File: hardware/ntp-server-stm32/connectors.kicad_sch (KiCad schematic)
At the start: 31 parts, among them J10 Conn_01x02_Pin, J11 Conn_01x08_Pin, J2 Conn_01x04_Pin, J3 Conn_01x06_Pin, J4 Conn_01x14_Pin, J5 USB4120-03-C_REVA6, J6 DE9_Socket_MountingHoles, J7 Conn_Coaxial, J8 Conn_Coaxial, J9 Conn_Coaxial, U15 TPD4E02B04DQAR, U16 TPD4E02B04DQAR, U17 TPD4E05U06DQAR, U18 TPD4E05U06DQAR, U19 TPD4E02B04DQAR, U20 TPD4E02B04DQAR

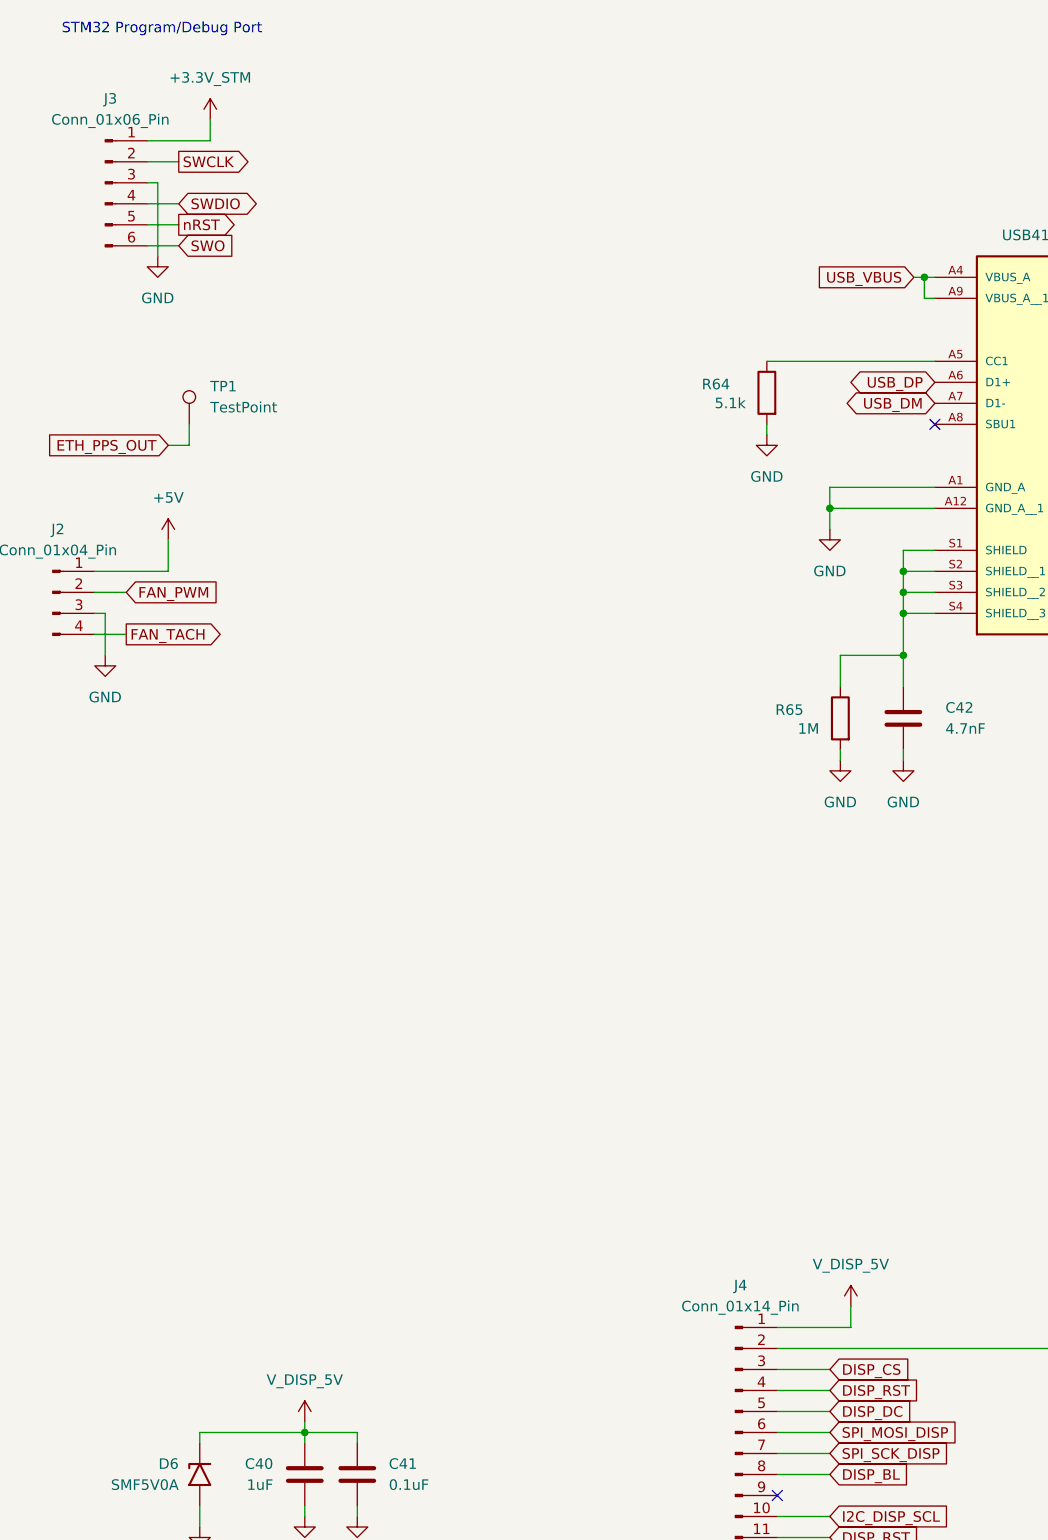
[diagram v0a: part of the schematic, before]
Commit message: Standardize net/rail names: plain 3V3 style, _N active-low, voltage-format PG/alerts
22 net renames applied across all sheets and verified: removed/added net-name
sets match intent exactly and all node connectivity is preserved (kicad-cli
netlist re-parse).

Co-Authored-By: Claude Opus 4.8 (1M context) <noreply@anthropic.com>
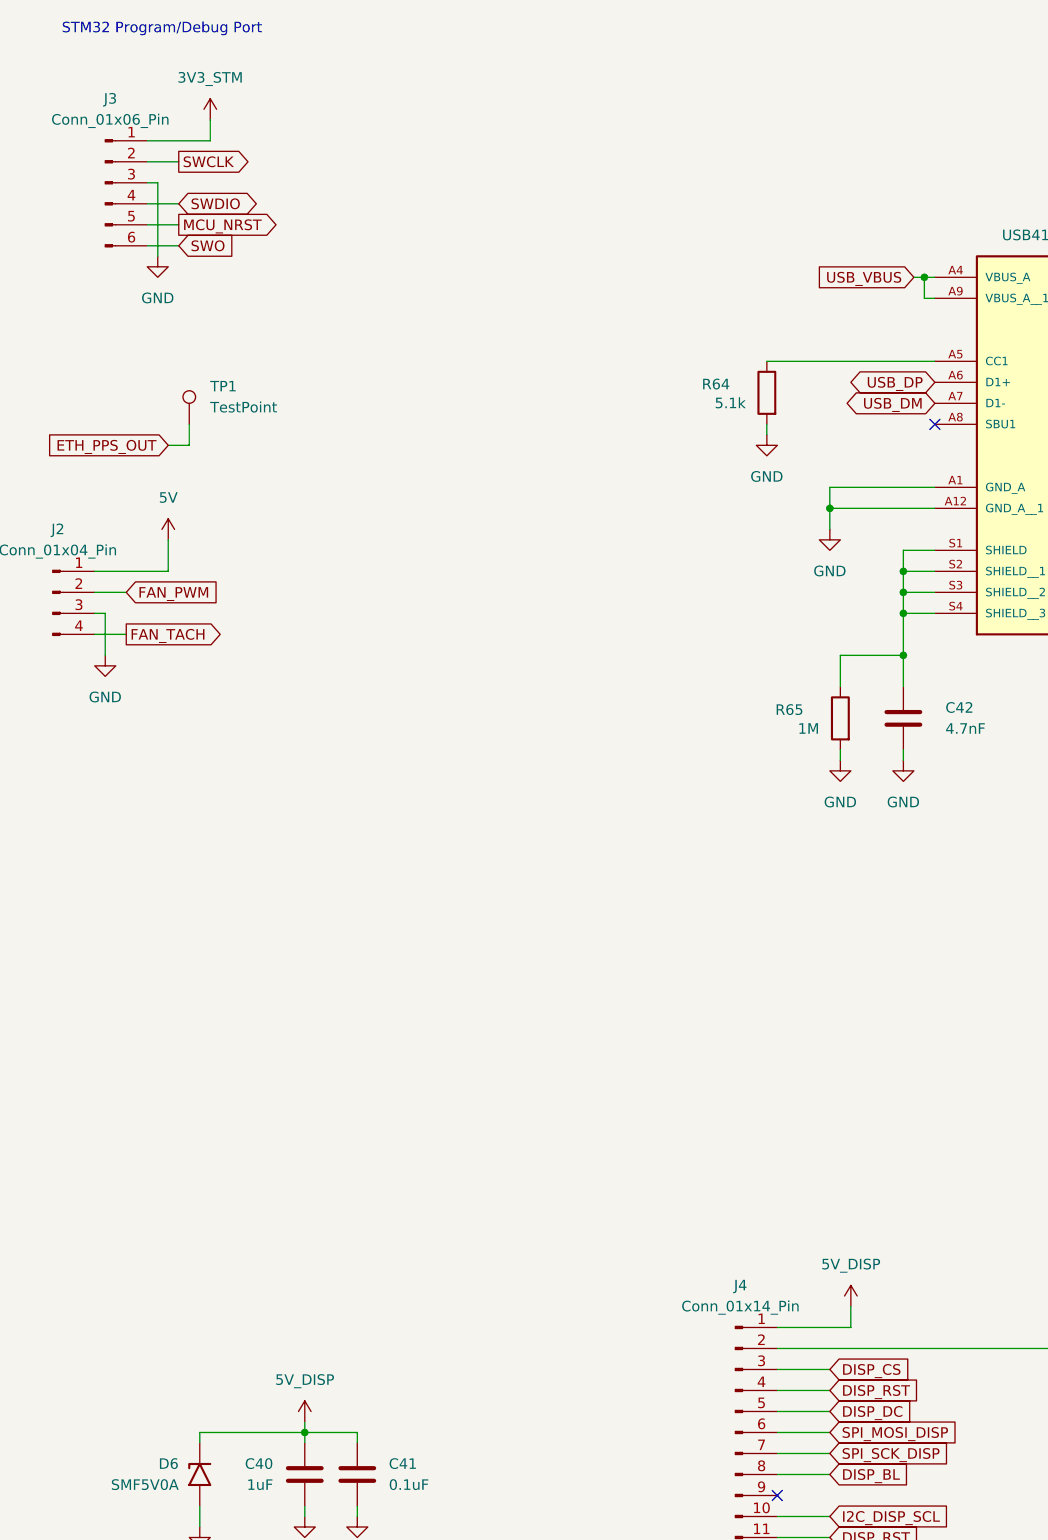
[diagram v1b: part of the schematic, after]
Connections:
- net +3.3V_STM renamed 3V3_STM
- net +5V renamed 5V
- net V_DISP_5V renamed 5V_DISP
- net nRST renamed MCU_NRST
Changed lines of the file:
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@@
 		)
 	)
-	(global_label "nRST"
+	(global_label "MCU_NRST"
 		(shape output)
 		(at 36.83 45.72 0)
@@
 			)
 		)
-		(property "Value" "+5V"
+		(property "Value" "5V"
 			(at 35.56 78.74 0)
 			(show_name no)
@@
 			)
 		)
-		(property "Value" "V_DISP_5V"
+		(property "Value" "5V_DISP"
 			(at 118.11 171.45 0)
 			(show_name no)
@@
 			)
 		)
-		(property "Value" "V_DISP_5V"
+		(property "Value" "5V_DISP"
 			(at 52.07 185.42 0)
 			(show_name no)
@@
 			)
 		)
-		(property "Value" "+3.3V_STM"
+		(property "Value" "3V3_STM"
 			(at 40.64 27.94 0)
 			(show_name no)

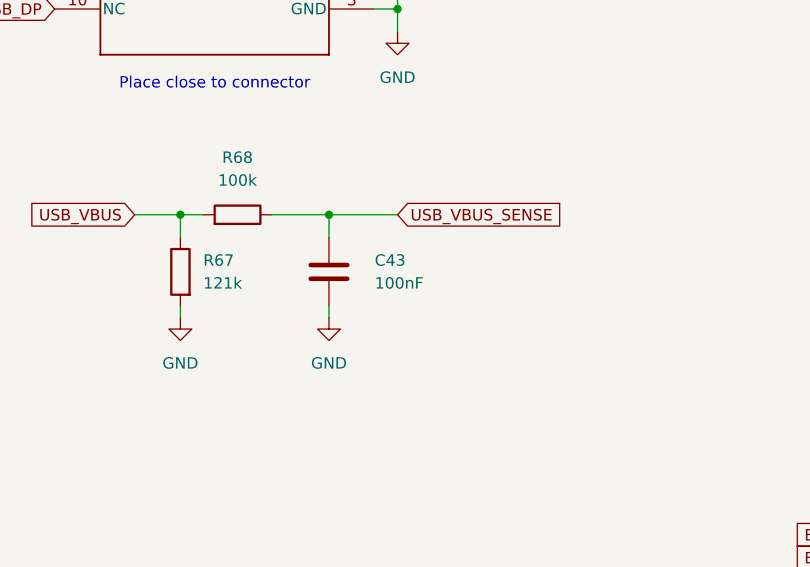
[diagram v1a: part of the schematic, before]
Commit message: Standardize + complete BOM; write fields back into KiCad symbols
- New sts1000_bom.csv: rebuilt from authoritative Value field (source MPN/footprint/
  description were corrupted by copy-paste). 338 standardized, 78 MPN-from-value,
  50 kept, ~64 flagged (SELECT/REVIEW-HV/SHUNT-REVIEW) each with full spec.
- Resistors -> deterministic Panasonic ERJ-2RKF 0402 1% 1/10W (consolidated 1 part/value).
- Caps -> verified Murata GRM parts where value matches; clean spec + footprint otherwise.
- 1633 symbol field updates (Value/Footprint/Description/MPN/Mfr/Digikey) written to
  .kicad_sch; netlist re-parse confirms connectivity byte-identical.
- Add docs/sts1000_net_naming.md naming reference.

Co-Authored-By: Claude Opus 4.8 (1M context) <noreply@anthropic.com>
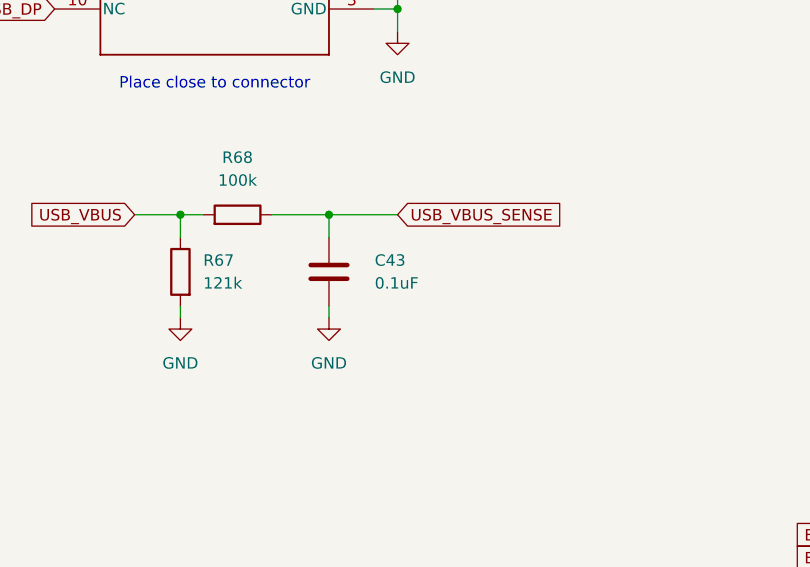
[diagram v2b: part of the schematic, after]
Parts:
- C40: footprint (none) -> C_0603_1608Metric
- C41: footprint (none) -> C_0402_1005Metric; DIGIKEY_PART_NUMBER (none) -> 490-6328-2-ND; MANUFACTURER (none) -> Murata; MANUFACTURER_PART_NUMBER (none) -> GRM155R71C104KA88J
- C42: footprint 0805 -> C_0402_1005Metric; DIGIKEY_PART_NUMBER 445-5972-1-ND -> 490-6334-2-ND; MANUFACTURER TDK -> Murata; MANUFACTURER_PART_NUMBER C2012X7R1E475K125AB -> GRM155R71C472KA01D
- C43: value 100nF -> 0.1uF; footprint 0805 -> C_0402_1005Metric; DIGIKEY_PART_NUMBER 445-5972-1-ND -> 490-6328-2-ND; MANUFACTURER TDK -> Murata; MANUFACTURER_PART_NUMBER C2012X7R1E475K125AB -> GRM155R71C104KA88J
- C44: footprint 0805 -> C_0402_1005Metric; DIGIKEY_PART_NUMBER 445-5972-1-ND -> 490-GRM1555C1H102FA01JTR-ND; MANUFACTURER TDK -> Murata; MANUFACTURER_PART_NUMBER C2012X7R1E475K125AB -> GRM1555C1H102FA01J
- D6: MANUFACTURER_PART_NUMBER (none) -> SMF5V0A
- D8, D9: MANUFACTURER_PART_NUMBER (none) -> SZESD7410MXWT5G
- J3: MANUFACTURER (none) -> GCT
- J5: MANUFACTURER_PART_NUMBER (none) -> USB4120-03-C_REVA6
- R64, R66: footprint (none) -> R_0402_1005Metric; MANUFACTURER (none) -> Panasonic; MANUFACTURER_PART_NUMBER (none) -> ERJ-2RKF5101X
- R65: footprint (none) -> R_0402_1005Metric; MANUFACTURER (none) -> Panasonic; MANUFACTURER_PART_NUMBER (none) -> ERJ-2RKF1004X
- R67: footprint (none) -> R_0402_1005Metric; MANUFACTURER (none) -> Panasonic; MANUFACTURER_PART_NUMBER (none) -> ERJ-2RKF1213X
- R68: footprint (none) -> R_0402_1005Metric; MANUFACTURER (none) -> Panasonic; MANUFACTURER_PART_NUMBER (none) -> ERJ-2RKF1003X
- U15, U16, U19, U20: MANUFACTURER_PART_NUMBER (none) -> TPD4E02B04DQAR
- U17, U18: MANUFACTURER_PART_NUMBER (none) -> TPD4E05U06DQAR
